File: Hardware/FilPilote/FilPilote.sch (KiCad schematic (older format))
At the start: 15 parts, among them J1 Conn_01x04_Male, P1 CONN_01X03, SW1 RESET, SW2 FLASH, U1 MOC3041M, U2 MOC3041M, U4 ESP-12E, U5 HLK-PM03

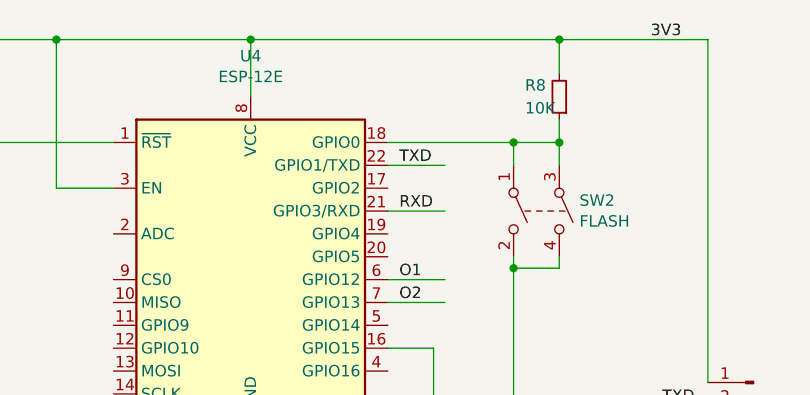
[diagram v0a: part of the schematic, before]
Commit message: - Modified almost all hardware boards : They were missing a pull-up resistor on GPIO2, which made impossible to flash. - Updated baseBoard.* files
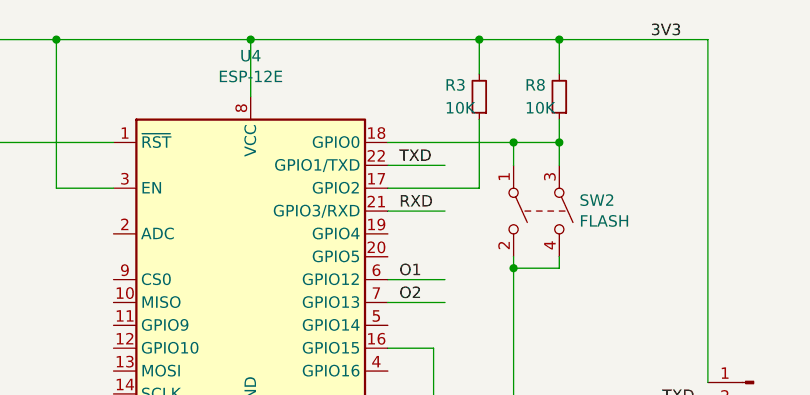
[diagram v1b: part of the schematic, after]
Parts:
- added R3: 10K, Resistor_SMD:R_0805_2012Metric_Pad1.15x1.40mm_HandSolder, symbol Device:R_Small
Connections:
- wire segments 67 -> 71
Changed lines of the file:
@@
 Connection ~ 2950 750
 Wire Wire Line
-	2950 750  4300 750
+	2950 750  3950 750
 Wire Wire Line
 	3550 1200 4100 1200
@@
 Wire Wire Line
 	2900 3300 3550 3300
+$Comp
+L Device:R_Small R3
+U 1 1 5C8005D7
+P 3950 1000
+F 0 "R3" H 4100 950 50  0000 R CNN
+F 1 "10K" H 4100 1050 50  0000 R CNN
+F 2 "Resistor_SMD:R_0805_2012Metric_Pad1.15x1.40mm_HandSolder" H 3950 1000 50  0001 C CNN
+F 3 "~" H 3950 1000 50  0001 C CNN
+	1    3950 1000
+	-1   0    0    1
+$EndComp
+Wire Wire Line
+	3950 900  3950 750
+Connection ~ 3950 750
+Wire Wire Line
+	3950 750  4300 750
+Wire Wire Line
+	3950 1100 3950 1400
+Wire Wire Line
+	3950 1400 3550 1400
 $EndSCHEMATC
